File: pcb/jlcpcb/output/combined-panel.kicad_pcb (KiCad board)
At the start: 2 copper layers, 128.5 x 150.1 mm, 154 parts, among them J101 FTSH-106-01-L-D-K, J201 Conn_01x06_MountingPin, J202 FTSH-106-01-L-D-K, SW10 SW_Push, SW11 SW_Push, SW12 SW_Push, SW13 SW_Push, SW15 SW_Push, SW16 SW_Push, SW17 SW_Push, SW18 SW_Push, SW19 SW_Push, SW20 SW_Push, SW22 SW_Push, SW23 SW_Push, SW24 SW_Push, SW25 SW_Push, SW26 SW_Push, SW27 SW_Push, SW28 SW_Push, SW29 SW_Push, SW30 SW_Push, SW31 SW_Push, SW32 SW_Push, SW33 SW_Push, SW34 SW_Push, SW35 SW_Push, SW43 SW_Push, SW44 SW_Push, SW45 SW_Push, SW46 SW_Push, SW47 SW_Push, SW48 SW_Push, SW50 SW_Push, SW51 SW_Push, SW52 SW_Push, SW53 SW_Push, SW54 SW_Push, SW55 SW_Push, SW57 SW_Push, SW58 SW_Push, SW59 SW_Push, SW60 SW_Push, SW61 SW_Push, SW62 SW_Push, SW64 SW_Push, SW65 SW_Push, SW69 SW_Push, SW70 SW_Push, SW8 SW_Push, SW9 SW_Push, U201 XIAO nRF52840 Plus

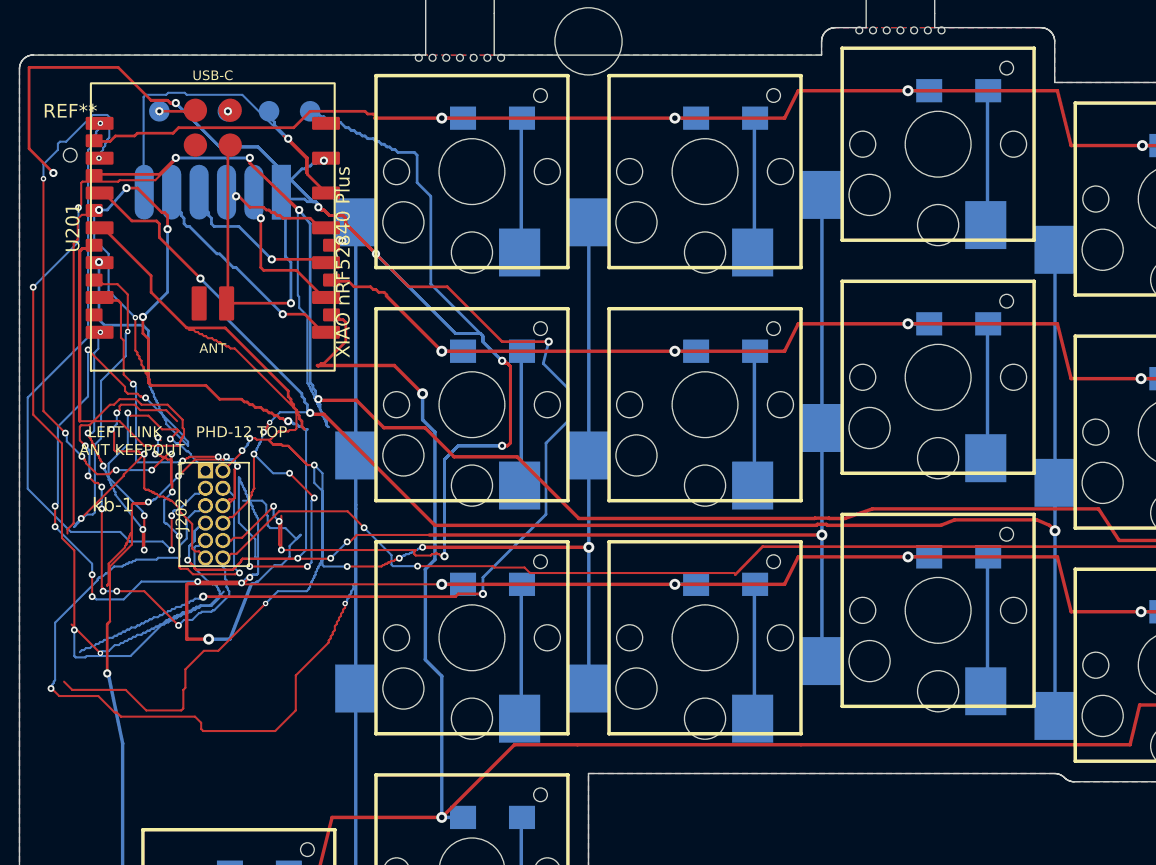
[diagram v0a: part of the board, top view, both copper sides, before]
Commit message: Improve XIAO and trackball adapter solder access
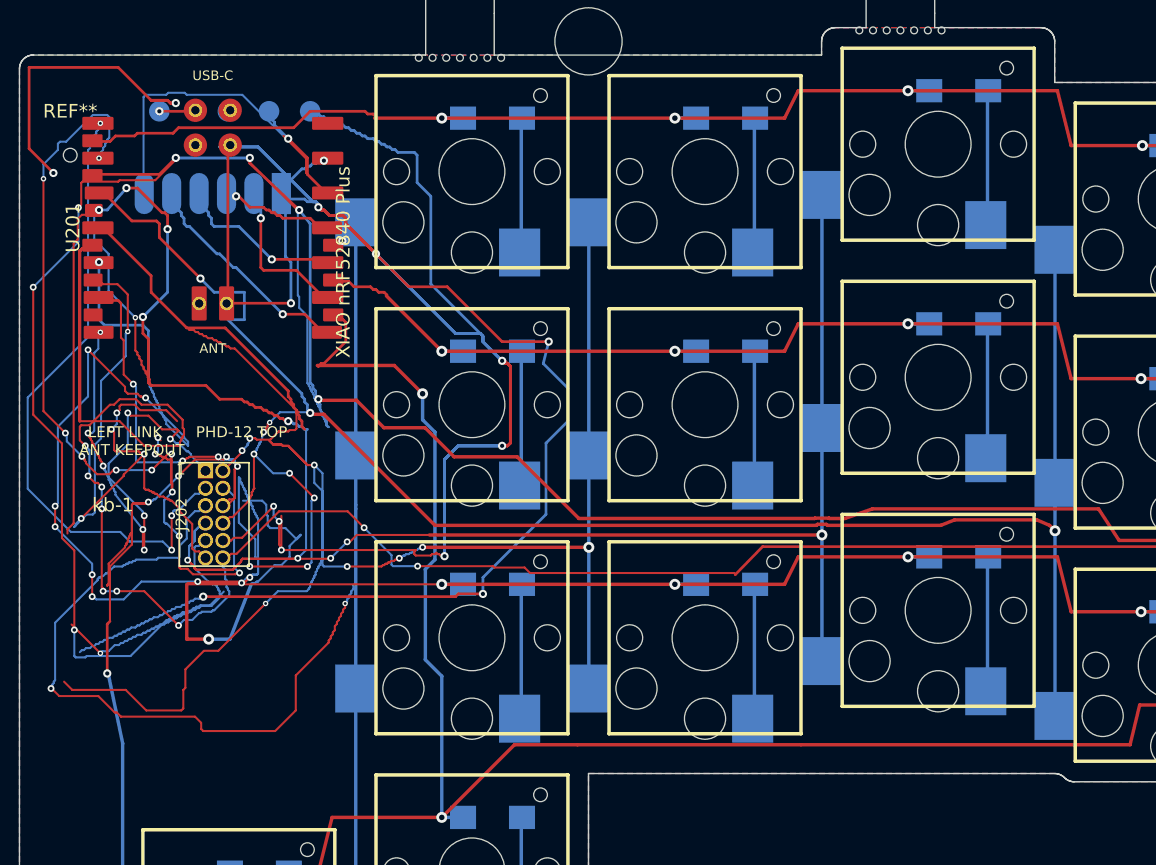
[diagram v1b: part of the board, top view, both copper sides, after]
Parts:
- moved J201 0.10 mm to (49.9, 101.2)
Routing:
- net Board_1-GND: track 298.3 -> 289.2 mm
- net Board_1-/right/COL2: track 143.5 -> 146.4 mm
- net Board_1-/right/SWDCLK: track 0.28 -> 0.00 mm, vias 1 -> 0

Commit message: Add routed screw reliefs to both PCBs and panel
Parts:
- removed the REF** at (77.2, 90.1)
- removed the REF** at (122.8, 14.0)
- removed the REF** at (37.8, 18.0)
- removed the REF** at (162.2, 94.1)
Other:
- outline, holes or cut-outs redrawn

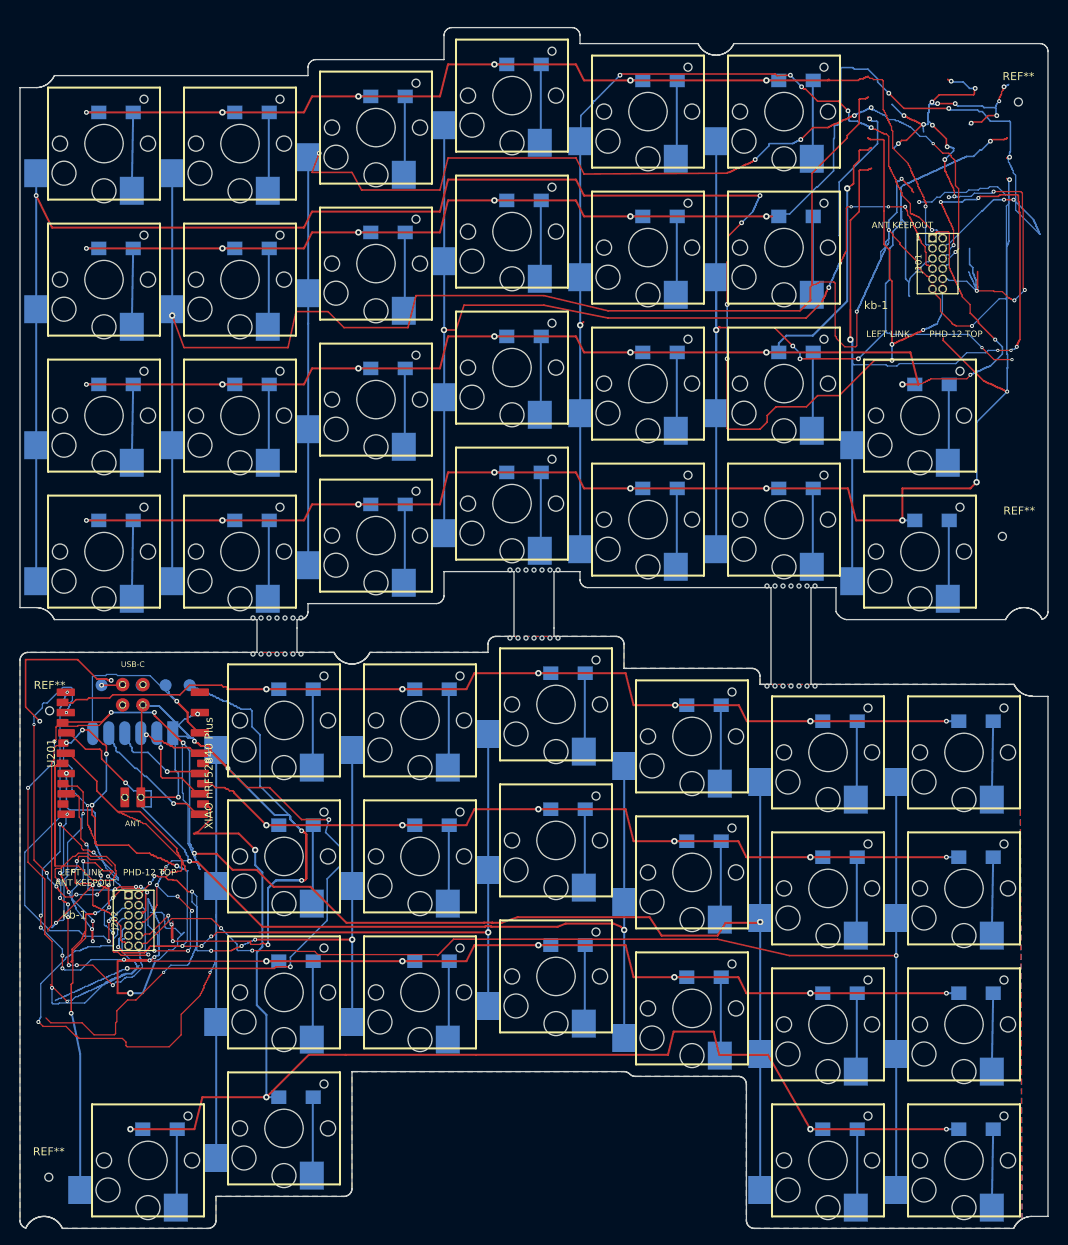
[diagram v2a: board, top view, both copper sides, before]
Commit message: Use standard 0.3 mm vias for JLCPCB panels
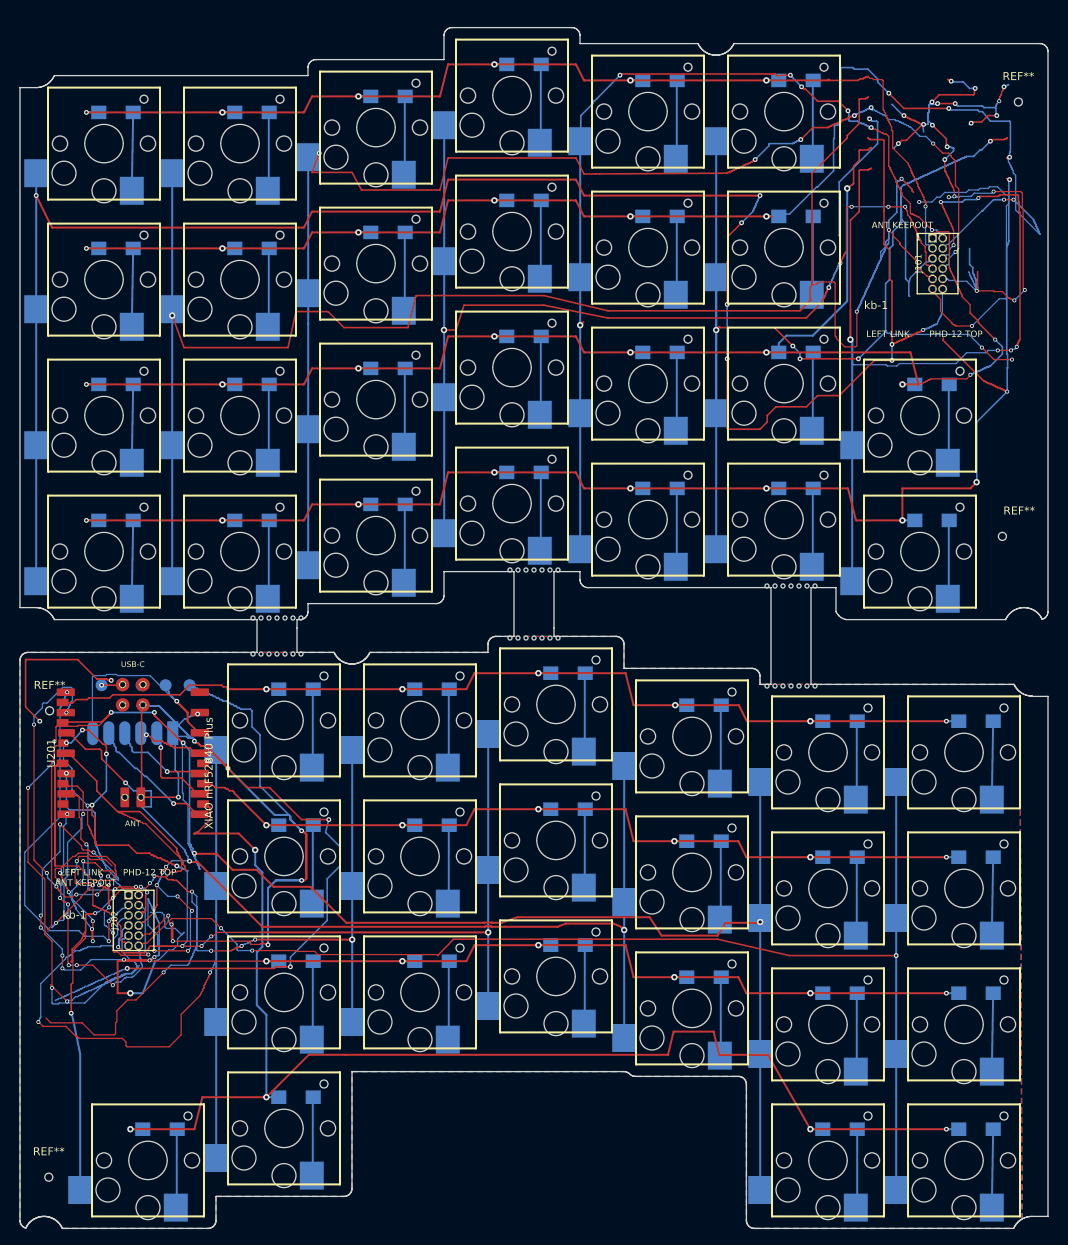
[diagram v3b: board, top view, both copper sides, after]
